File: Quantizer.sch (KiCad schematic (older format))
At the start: 39 parts, among them J1 CV, J2 SlideCV, J3 trigger, J4 AudioJack2_SwitchT, J5 Conn_02x05_Odd_Even, SW1 Rotary_Encoder, SW2 SW_SPDT, U1 MCP4821, U2 L7805

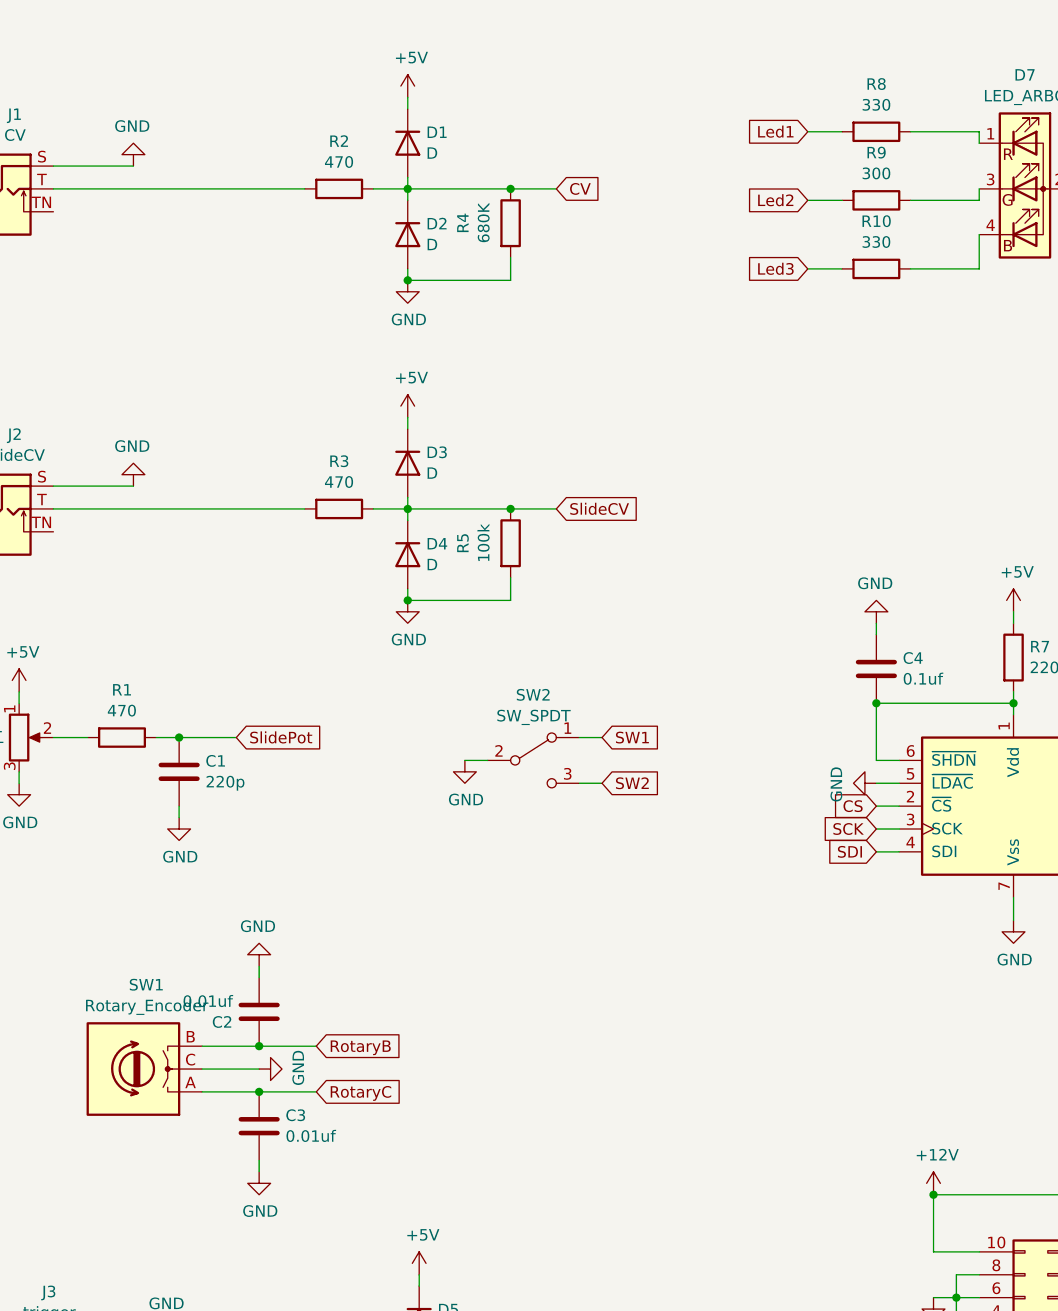
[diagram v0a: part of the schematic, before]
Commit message: updated Ibom and values capacitors
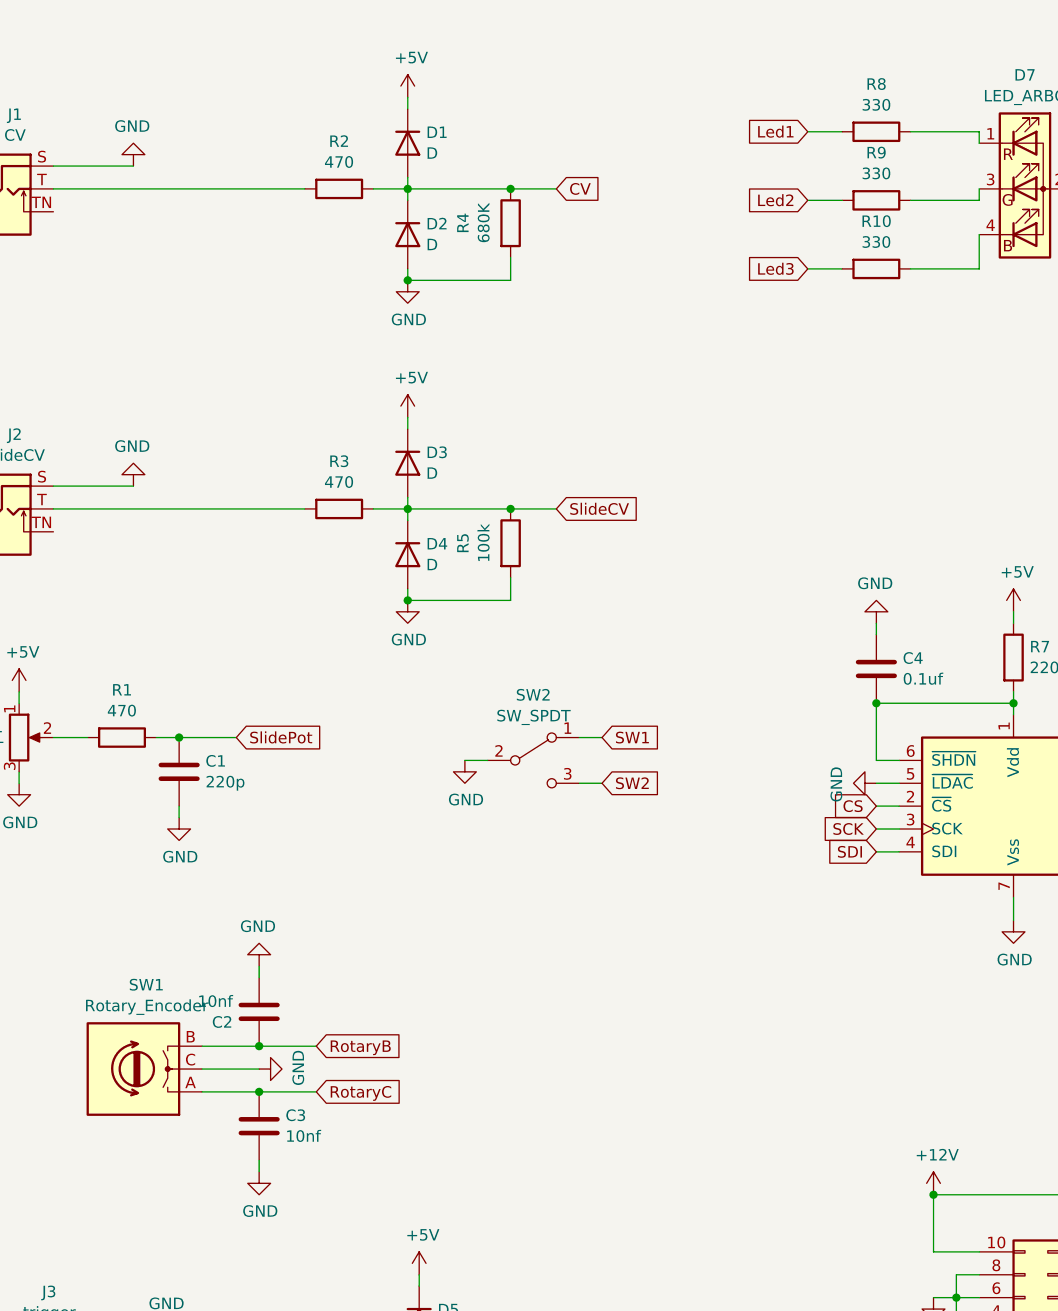
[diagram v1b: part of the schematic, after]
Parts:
- C2, C3: value 0.01uf -> 10nf
- R9: value 300 -> 330
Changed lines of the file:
@@
 P 1950 4800
 F 0 "C2" H 2065 4846 50  0000 L CNN
-F 1 "0.01uf" H 2065 4755 50  0000 L CNN
+F 1 "10nf" H 2065 4755 50  0000 L CNN
 F 2 "Capacitor_THT:C_Disc_D3.8mm_W2.6mm_P2.50mm" H 1988 4650 50  0001 C CNN
 F 3 "~" H 1950 4800 50  0001 C CNN
@@
 P 1950 5300
 F 0 "C3" H 2065 5346 50  0000 L CNN
-F 1 "0.01uf" H 2065 5255 50  0000 L CNN
+F 1 "10nf" H 2065 5255 50  0000 L CNN
 F 2 "Capacitor_THT:C_Disc_D3.8mm_W2.6mm_P2.50mm" H 1988 5150 50  0001 C CNN
 F 3 "~" H 1950 5300 50  0001 C CNN
@@
 P 4650 1250
 F 0 "R9" V 4443 1250 50  0000 C CNN
-F 1 "300" V 4534 1250 50  0000 C CNN
+F 1 "330" V 4534 1250 50  0000 C CNN
 F 2 "Resistor_THT:R_Axial_DIN0207_L6.3mm_D2.5mm_P7.62mm_Horizontal" V 4580 1250 50  0001 C CNN
 F 3 "~" H 4650 1250 50  0001 C CNN
